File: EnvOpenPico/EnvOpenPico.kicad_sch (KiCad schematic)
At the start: 58 parts, among them J2 SKRKAEE020, J3 2.54mm header 01x20, J4 2.54mm header 01x20, J5 Conn_01x03_Male, Q1 Si2329DS, U1 TLV75533PDBVR, U3 RP2040, Y1 3225_4P

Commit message: tiny cleanup, generated updated gerbers
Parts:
- FB1: value FerriteBead -> FerriteBead 0402
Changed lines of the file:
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@@
     (in_bom yes) (on_board yes) (fields_autoplaced)
     (property "Reference" "FB1" (id 0) (at 90.1192 37.084 90))
-    (property "Value" "FerriteBead" (id 1) (at 90.1192 39.624 90))
+    (property "Value" "FerriteBead 0402" (id 1) (at 90.1192 39.624 90))
     (property "Footprint" "Resistor_SMD:R_0402_1005Metric" (id 2) (at 90.17 46.228 90)
       (effects (font (size 1.27 1.27)) hide)
@@
     )
     (path "/cb658bfb-bb44-442b-af68-cdf8168ed728"
-      (reference "FB1") (unit 1) (value "FerriteBead") (footprint "Resistor_SMD:R_0402_1005Metric")
+      (reference "FB1") (unit 1) (value "FerriteBead 0402") (footprint "Resistor_SMD:R_0402_1005Metric")
     )
     (path "/00000000-0000-0000-0000-0000608edada"

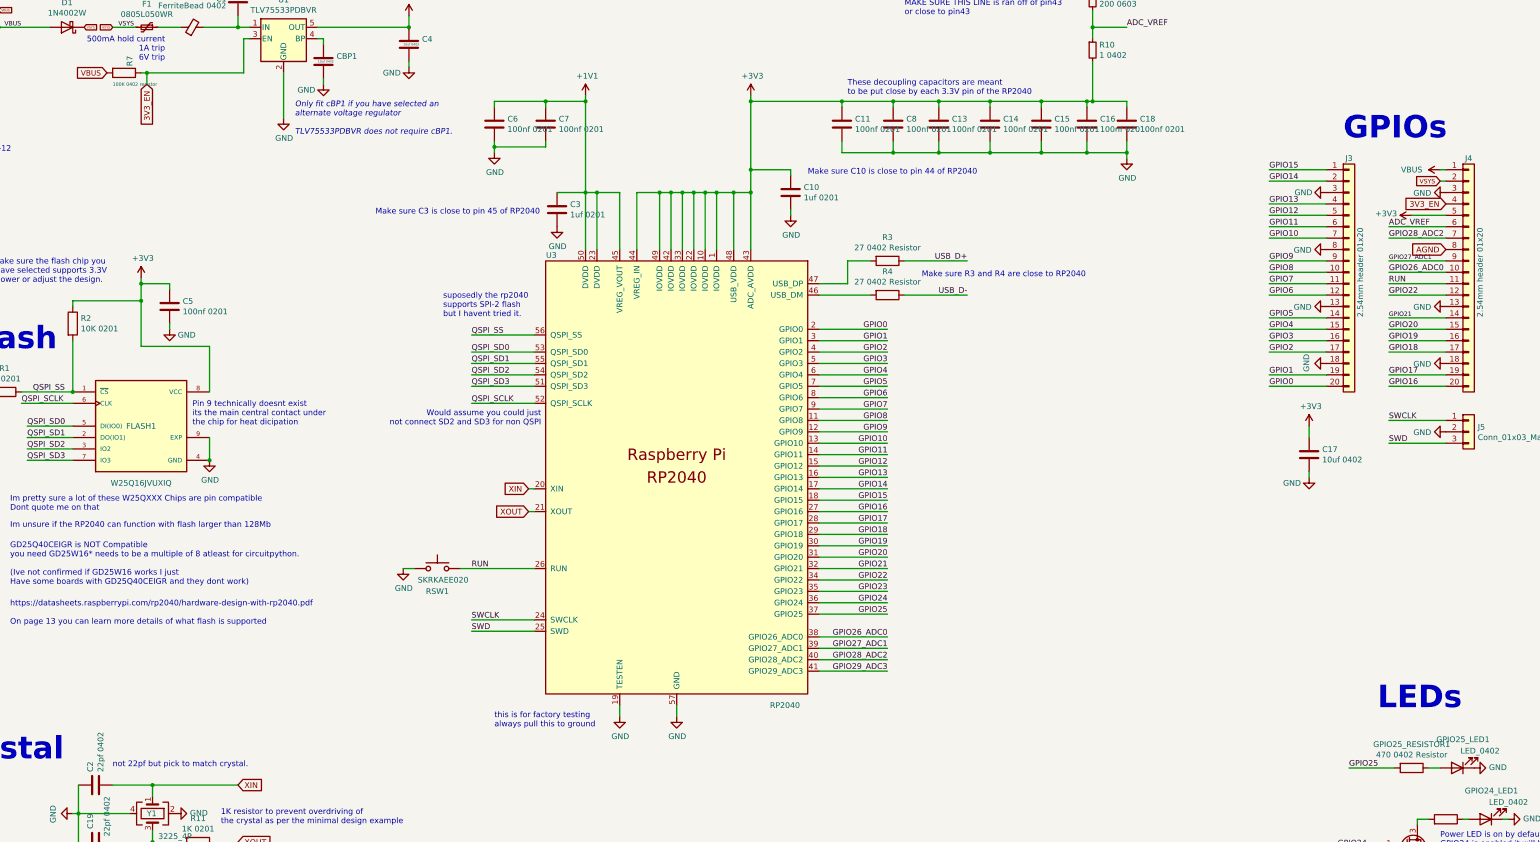
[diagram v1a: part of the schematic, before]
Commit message: swapped out a 10K 0201 for a 10K 0402
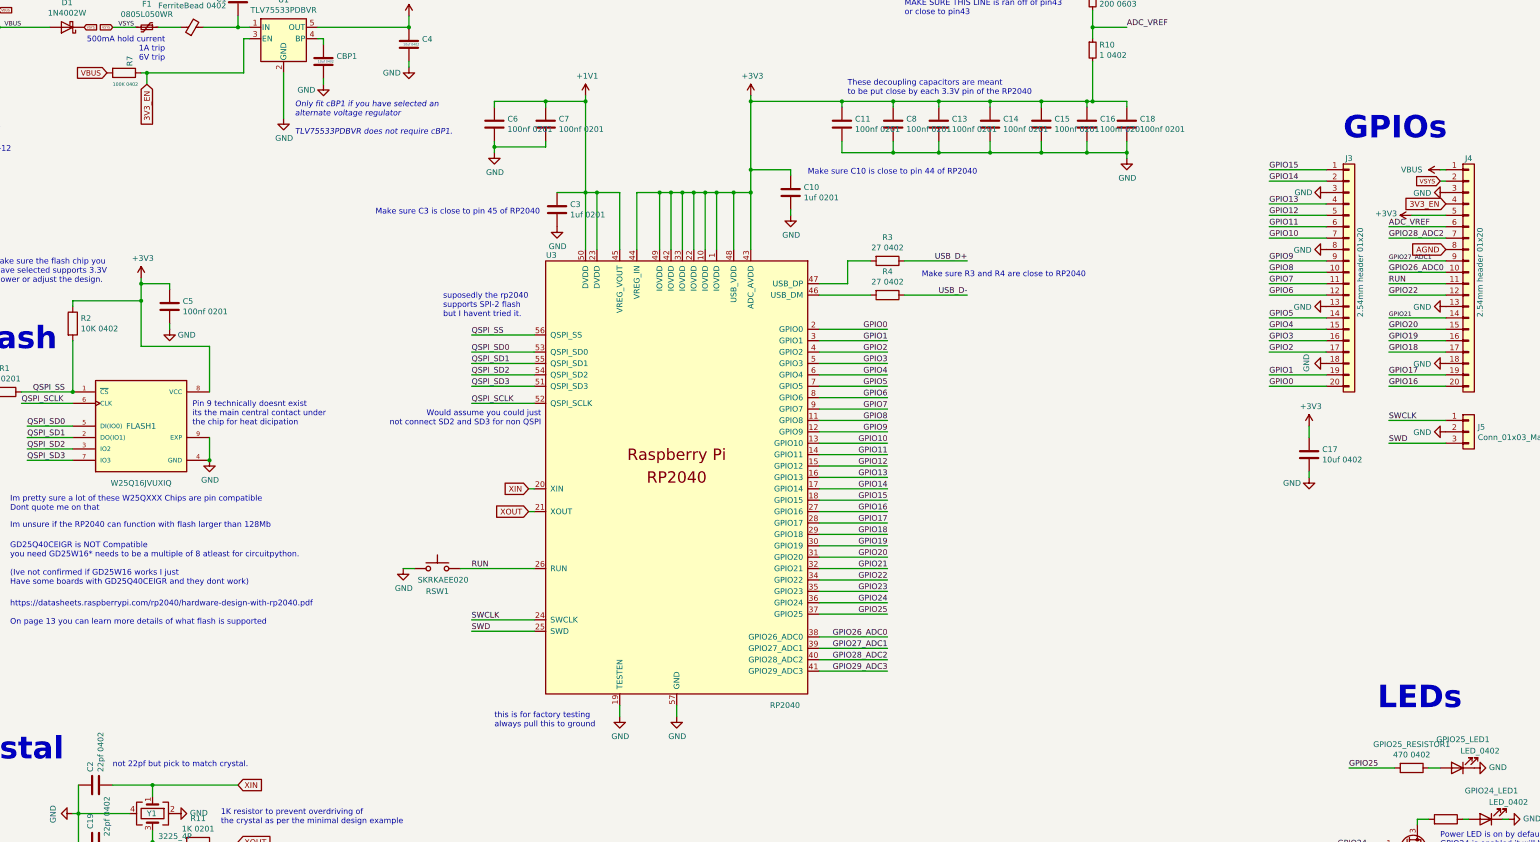
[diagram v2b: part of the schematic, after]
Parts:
- GPIO24_RESISTOR1, GPIO25_RESISTOR1: value 470 0402 Resistor -> 470 0402
- R1, R11: footprint Capacitor_SMD:C_0201_0603Metric -> Resistor_SMD:R_0201_0603Metric
- R2: value 10K 0201 -> 10K 0402; footprint Capacitor_SMD:C_0201_0603Metric -> Resistor_SMD:R_0402_1005Metric
- R3, R4: value 27 0402 Resistor -> 27 0402
- R7: value 100K 0402 resistor -> 100K 0402
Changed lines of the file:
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@@
       (effects (font (size 1.27 1.27)) (justify left))
     )
-    (property "Value" "10K 0201" (id 1) (at 65.278 111.633 0)
-      (effects (font (size 1.27 1.27)) (justify left))
-    )
-    (property "Footprint" "Capacitor_SMD:C_0201_0603Metric" (id 2) (at 61.722 110.49 90)
+    (property "Value" "10K 0402" (id 1) (at 65.278 111.633 0)
+      (effects (font (size 1.27 1.27)) (justify left))
+    )
+    (property "Footprint" "Resistor_SMD:R_0402_1005Metric" (id 2) (at 61.722 110.49 90)
       (effects (font (size 1.27 1.27)) hide)
     )
@@
     (property "Reference" "R1" (id 0) (at 48.26 120.4722 90))
     (property "Value" "1K 0201" (id 1) (at 48.26 122.7836 90))
-    (property "Footprint" "Capacitor_SMD:C_0201_0603Metric" (id 2) (at 48.26 123.952 90)
+    (property "Footprint" "Resistor_SMD:R_0201_0603Metric" (id 2) (at 48.26 123.952 90)
       (effects (font (size 1.27 1.27)) hide)
     )
@@
     (in_bom yes) (on_board yes)
     (property "Reference" "R3" (id 0) (at 245.11 91.2622 90))
-    (property "Value" "27 0402 Resistor" (id 1) (at 245.11 93.5736 90))
+    (property "Value" "27 0402" (id 1) (at 245.11 93.5736 90))
     (property "Footprint" "Resistor_SMD:R_0402_1005Metric" (id 2) (at 245.11 94.742 90)
       (effects (font (size 1.27 1.27)) hide)
@@
     (in_bom yes) (on_board yes)
     (property "Reference" "R4" (id 0) (at 245.11 98.8822 90))
-    (property "Value" "27 0402 Resistor" (id 1) (at 245.11 101.1936 90))
+    (property "Value" "27 0402" (id 1) (at 245.11 101.1936 90))
     (property "Footprint" "Resistor_SMD:R_0402_1005Metric" (id 2) (at 245.11 102.362 90)
       (effects (font (size 1.27 1.27)) hide)
@@
       (effects (font (size 1.27 1.27)) (justify left))
     )
-    (property "Value" "100K 0402 resistor" (id 1) (at 72.39 57.15 90)
+    (property "Value" "100K 0402" (id 1) (at 72.39 57.15 90)
       (effects (font (size 0.762 0.762)) (justify left))
     )
@@
     (in_bom yes) (on_board yes)
     (property "Reference" "GPIO25_RESISTOR1" (id 0) (at 361.95 204.2922 90))
-    (property "Value" "470 0402 Resistor" (id 1) (at 361.95 206.6036 90))
+    (property "Value" "470 0402" (id 1) (at 361.95 206.6036 90))
     (property "Footprint" "Resistor_SMD:R_0402_1005Metric" (id 2) (at 361.95 207.772 90)
       (effects (font (size 1.27 1.27)) hide)
@@
     (property "Reference" "R11" (id 0) (at 91.44 220.8022 90))
     (property "Value" "1K 0201" (id 1) (at 91.44 223.1136 90))
-    (property "Footprint" "Capacitor_SMD:C_0201_0603Metric" (id 2) (at 91.44 224.282 90)
+    (property "Footprint" "Resistor_SMD:R_0201_0603Metric" (id 2) (at 91.44 224.282 90)
       (effects (font (size 1.27 1.27)) hide)
     )
@@
       (effects (font (size 1.27 1.27)) hide)
     )
-    (property "Value" "470 0402 Resistor" (id 1) (at 369.57 223.9264 90)
+    (property "Value" "470 0402" (id 1) (at 369.57 223.9264 90)
       (effects (font (size 1.27 1.27)) hide)
     )
@@
     )
     (path "/00000000-0000-0000-0000-000061cabb24"
-      (reference "GPIO24_RESISTOR1") (unit 1) (value "470 0402 Resistor") (footprint "Resistor_SMD:R_0402_1005Metric")
+      (reference "GPIO24_RESISTOR1") (unit 1) (value "470 0402") (footprint "Resistor_SMD:R_0402_1005Metric")
     )
     (path "/00000000-0000-0000-0000-000060cc7b32"
@@
     )
     (path "/00000000-0000-0000-0000-000060cc69df"
-      (reference "GPIO25_RESISTOR1") (unit 1) (value "470 0402 Resistor") (footprint "Resistor_SMD:R_0402_1005Metric")
+      (reference "GPIO25_RESISTOR1") (unit 1) (value "470 0402") (footprint "Resistor_SMD:R_0402_1005Metric")
     )
     (path "/00000000-0000-0000-0000-00005ef4c292"
@@
     )
     (path "/00000000-0000-0000-0000-00005edae9f0"
-      (reference "R1") (unit 1) (value "1K 0201") (footprint "Capacitor_SMD:C_0201_0603Metric")
+      (reference "R1") (unit 1) (value "1K 0201") (footprint "Resistor_SMD:R_0201_0603Metric")
     )
     (path "/00000000-0000-0000-0000-00005edac067"
-      (reference "R2") (unit 1) (value "10K 0201") (footprint "Capacitor_SMD:C_0201_0603Metric")
+      (reference "R2") (unit 1) (value "10K 0402") (footprint "Resistor_SMD:R_0402_1005Metric")
     )
     (path "/00000000-0000-0000-0000-00005ede0881"
-      (reference "R3") (unit 1) (value "27 0402 Resistor") (footprint "Resistor_SMD:R_0402_1005Metric")
+      (reference "R3") (unit 1) (value "27 0402") (footprint "Resistor_SMD:R_0402_1005Metric")
     )
     (path "/00000000-0000-0000-0000-00005ede1624"
-      (reference "R4") (unit 1) (value "27 0402 Resistor") (footprint "Resistor_SMD:R_0402_1005Metric")
+      (reference "R4") (unit 1) (value "27 0402") (footprint "Resistor_SMD:R_0402_1005Metric")
     )
     (path "/00000000-0000-0000-0000-00006093a5b0"
@@
     )
     (path "/00000000-0000-0000-0000-0000608cfaf0"
-      (reference "R7") (unit 1) (value "100K 0402 resistor") (footprint "Resistor_SMD:R_0402_1005Metric")
+      (reference "R7") (unit 1) (value "100K 0402") (footprint "Resistor_SMD:R_0402_1005Metric")
     )
     (path "/00000000-0000-0000-0000-000061044b24"
@@
     )
     (path "/00000000-0000-0000-0000-00006150e6ab"
-      (reference "R11") (unit 1) (value "1K 0201") (footprint "Capacitor_SMD:C_0201_0603Metric")
+      (reference "R11") (unit 1) (value "1K 0201") (footprint "Resistor_SMD:R_0201_0603Metric")
     )
     (path "/00000000-0000-0000-0000-00006142c001"

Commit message: swapped some parts back to 0402 size due to stock issues among fixes.
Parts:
- C1: value 10uf 402 -> (none); footprint Capacitor_SMD:C_0402_1005Metric -> (none)
- C10, C3: value 1uf 0201 -> (none); footprint Capacitor_SMD:C_0201_0603Metric -> (none)
- C11, C13, C14, C15, C16, C18, C5, C6, C7, C8: value 100nf 0201 -> (none); footprint Capacitor_SMD:C_0201_0603Metric -> (none)
- C17, C4, CBP1: value 10uf 0402 -> (none); footprint Capacitor_SMD:C_0402_1005Metric -> (none)
- C19, C2: value 22pf 0402 -> (none); footprint Capacitor_SMD:C_0402_1005Metric -> (none)
- D1: value 1N4002W -> (none); footprint Diode_SMD:D_SOD-123 -> (none)
- F1: value 0805L050WR -> (none); footprint Fuse:Fuse_0805_2012Metric -> (none)
- FB1: value FerriteBead 0402 -> (none); footprint Resistor_SMD:R_0402_1005Metric -> (none)
- FLASH1: value W25Q16JVUXIQ -> (none); footprint Package_SON:SON-8-1EP_3x2mm_P0.5mm_EP1.4x1.6mm -> (none)
- GPIO24_LED1, GPIO25_LED1: value LED_0402 -> (none); footprint LED_SMD:LED_0402_1005Metric -> (none)
- GPIO24_RESISTOR1, GPIO25_RESISTOR1: value 470 0402 -> (none); footprint Resistor_SMD:R_0402_1005Metric -> (none)
- H1, H2, H3, H4: value MountingHole -> (none); footprint MountingHole:MountingHole_2.2mm_M2 -> (none)
- J2, RSW1: value SKRKAEE020 -> (none); footprint Button_Switch_SMD:SW_Push_SPST_NO_Alps_SKRK -> (none)
- J3, J4: value 2.54mm header 01x20 -> (none); footprint Connector_PinHeader_2.54mm:PinHeader_1x20_P2.54mm_Vertical -> (none)
- J5: value Conn_01x03_Male -> (none); footprint Connector_PinHeader_2.54mm:PinHeader_1x03_P2.54mm_Vertical -> (none)
- NT1: value NetTie_2 -> (none); footprint NetTie:NetTie-2_SMD_Pad0.5mm -> (none)
- Q1: value Si2329DS -> (none); footprint Package_TO_SOT_SMD:SOT-23 -> (none)
- R1, R11: value 1K 0201 -> (none); footprint Resistor_SMD:R_0201_0603Metric -> (none)
- R10: value 1 0402 -> (none); footprint Resistor_SMD:R_0402_1005Metric -> (none)
- R2: value 10K 0402 -> (none); footprint Resistor_SMD:R_0402_1005Metric -> (none)
- R3, R4: value 27 0402 -> (none); footprint Resistor_SMD:R_0402_1005Metric -> (none)
- R5, R6: value 5.1K 0402 -> (none); footprint Resistor_SMD:R_0402_1005Metric -> (none)
- R7: value 100K 0402 -> (none); footprint Resistor_SMD:R_0402_1005Metric -> (none)
- R9: value 200 0603 -> (none); footprint Resistor_SMD:R_0603_1608Metric -> (none)
- TP1, TP2, TP3, TP4, TP6, TP7, TP8: value TestPoint -> (none); footprint EnvExtras:CustomTestPoint -> (none)
- U1: value TLV75533PDBVR -> (none); footprint Package_TO_SOT_SMD:SOT-23-5 -> (none)
- U3: value RP2040 -> (none); footprint RP2040_minimal:RP2040-QFN-56 -> (none)
- USB1: value TYPE-C-31-M-12 -> (none); footprint HRO-TYPE-C31-M-12:HRO-TYPE-C-31-M-12 -> (none)
- Y1: value 3225_4P -> (none); footprint Crystal:Crystal_SMD_3225-4Pin_3.2x2.5mm -> (none)

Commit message: added eeprom ic on GP29 and GP28
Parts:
- added R12, R8: 10K 0402 Resistor, Resistor_SMD:R_0402_1005Metric, symbol Device:R
- added U2: 24LC256, Package_DFN_QFN:TDFN-8-1EP_3x2mm_P0.5mm_EP1.3x1.4mm, symbol Memory_EEPROM:24LC256
- C1, C17, C4, CBP1: value (none) -> 10uf 0402; footprint (none) -> Capacitor_SMD:C_0402_1005Metric
- C10, C3: value (none) -> 1uf 0402; footprint (none) -> Capacitor_SMD:C_0402_1005Metric
- C11, C13, C14, C15, C16, C18, C5, C6, C7, C8: value (none) -> 100nf 0402; footprint (none) -> Capacitor_SMD:C_0402_1005Metric
- C19, C2: value (none) -> 22pf 0402; footprint (none) -> Capacitor_SMD:C_0402_1005Metric
- D1: value (none) -> 1N4002W; footprint (none) -> Diode_SMD:D_SOD-123
- F1: value (none) -> 0805L050WR; footprint (none) -> Fuse:Fuse_0805_2012Metric
- FB1: value (none) -> FerriteBead 0402; footprint (none) -> Resistor_SMD:R_0402_1005Metric
- FLASH1: value (none) -> W25Q16JVUXIQ; footprint (none) -> Package_SON:SON-8-1EP_3x2mm_P0.5mm_EP1.4x1.6mm
- GPIO24_LED1, GPIO25_LED1: value (none) -> LED_0402; footprint (none) -> LED_SMD:LED_0402_1005Metric
- GPIO24_RESISTOR1, GPIO25_RESISTOR1: value (none) -> 470 0402; footprint (none) -> Resistor_SMD:R_0402_1005Metric
- H1, H2, H3, H4: value (none) -> MountingHole; footprint (none) -> MountingHole:MountingHole_2.2mm_M2
- J2, RSW1: value (none) -> SKRKAEE020; footprint (none) -> Button_Switch_SMD:SW_Push_SPST_NO_Alps_SKRK
- J3, J4: value (none) -> 2.54mm header 01x20; footprint (none) -> Connector_PinHeader_2.54mm:PinHeader_1x20_P2.54mm_Vertical
- J5: value (none) -> Conn_01x03_Male; footprint (none) -> Connector_PinHeader_2.54mm:PinHeader_1x03_P2.54mm_Vertical
- NT1: value (none) -> NetTie_2; footprint (none) -> NetTie:NetTie-2_SMD_Pad0.5mm
- Q1: value (none) -> Si2329DS; footprint (none) -> Package_TO_SOT_SMD:SOT-23
- R1, R11: value (none) -> 1K 0201; footprint (none) -> Resistor_SMD:R_0201_0603Metric
- R10: value (none) -> 1 0402; footprint (none) -> Resistor_SMD:R_0402_1005Metric
- R2: value (none) -> 10K 0402; footprint (none) -> Resistor_SMD:R_0402_1005Metric
- R3, R4: value (none) -> 27 0402; footprint (none) -> Resistor_SMD:R_0402_1005Metric
- R5, R6: value (none) -> 5.1K 0402; footprint (none) -> Resistor_SMD:R_0402_1005Metric
- R7: value (none) -> 100K 0402; footprint (none) -> Resistor_SMD:R_0402_1005Metric
- R9: value (none) -> 200 0603; footprint (none) -> Resistor_SMD:R_0603_1608Metric
- TP1, TP2, TP3, TP4, TP6, TP7, TP8: value (none) -> TestPoint; footprint (none) -> EnvExtras:CustomTestPoint
- U1: value (none) -> TLV75533PDBVR; footprint (none) -> Package_TO_SOT_SMD:SOT-23-5
- U3: value (none) -> RP2040; footprint (none) -> RP2040_minimal:RP2040-QFN-56
- USB1: value (none) -> TYPE-C-31-M-12; footprint (none) -> HRO-TYPE-C31-M-12:HRO-TYPE-C-31-M-12
- Y1: value (none) -> 3225_4P; footprint (none) -> Crystal:Crystal_SMD_3225-4Pin_3.2x2.5mm
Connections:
- net +3V3: now also R12.1, R8.1, U2.8 (VCC)
- net GND: now also U2.1 (A0), U2.2 (A1), U2.3 (A2), U2.4 (GND), U2.7 (WP)
- net GPIO28_ADC2 renamed GP28-SDA
- net GP28-SDA: now also R8.2, U2.5 (SDA)
- net GPIO29_ADC3 renamed GP29-SCL
- net GP29-SCL: now also R12.2, U2.6 (SCL)
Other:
- note added: "EEPROM"
- note added: "smol EEPROM for QMK stuffs"
- moved on the sheet: C19, C2, R11, Y1

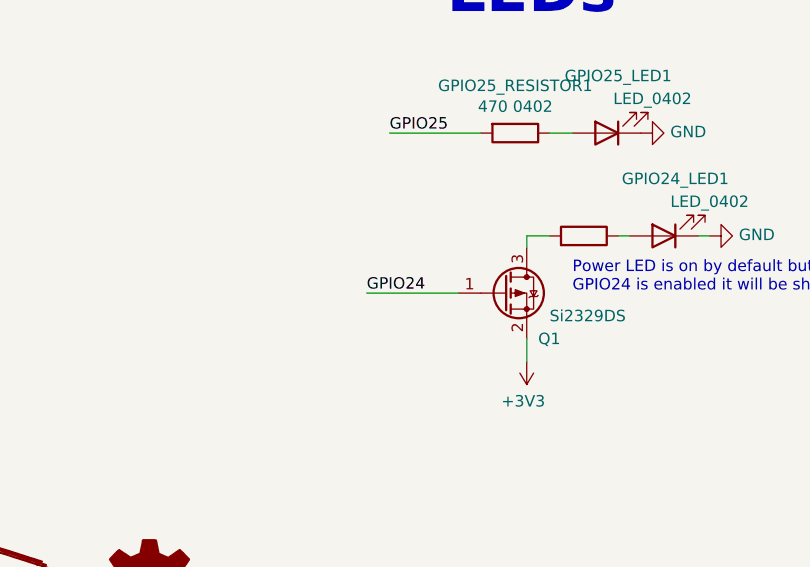
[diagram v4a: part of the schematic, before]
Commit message: some changes as per suggested by Sigprof of QMK Discord.
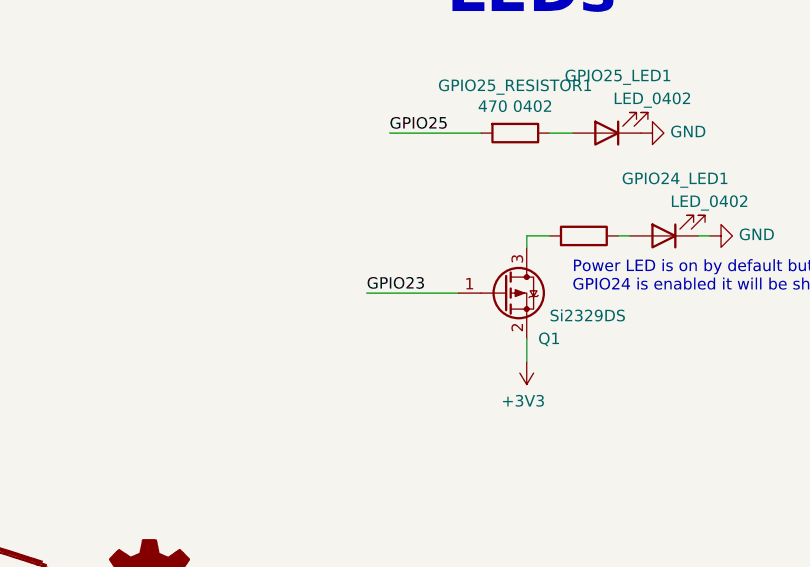
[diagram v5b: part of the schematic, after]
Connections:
- net GPIO23: now also Q1.1 (G)
- net GPIO24: no longer Q1.1 (G)
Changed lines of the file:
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@@
     (effects (font (size 1.27 1.27)) (justify left bottom))
   )
-  (label "GPIO24" (at 345.44 227.33 0)
+  (label "GPIO23" (at 345.44 227.33 0)
     (effects (font (size 1.27 1.27)) (justify left bottom))
   )
